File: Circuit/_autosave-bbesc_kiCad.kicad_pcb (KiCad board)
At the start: 2 copper layers, 81.4 x 63.5 mm, 82 parts, among them J1 CONN_01X06, J3 CONN_01X02, M3 -> 81.28mm MountingHole_3.2mm_M3_DIN965_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, M3 56.515mm Square MountingHole_3.2mm_M3_DIN965_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, M3 MountingHole_3.2mm_M3_DIN965_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, M3 offset inside by 3.429mm MountingHole_3.2mm_M3_DIN965_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, P2 CONN_01X03, P5 CONN_01X01, P6 CONN_01X01, P7 CONN_01X01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

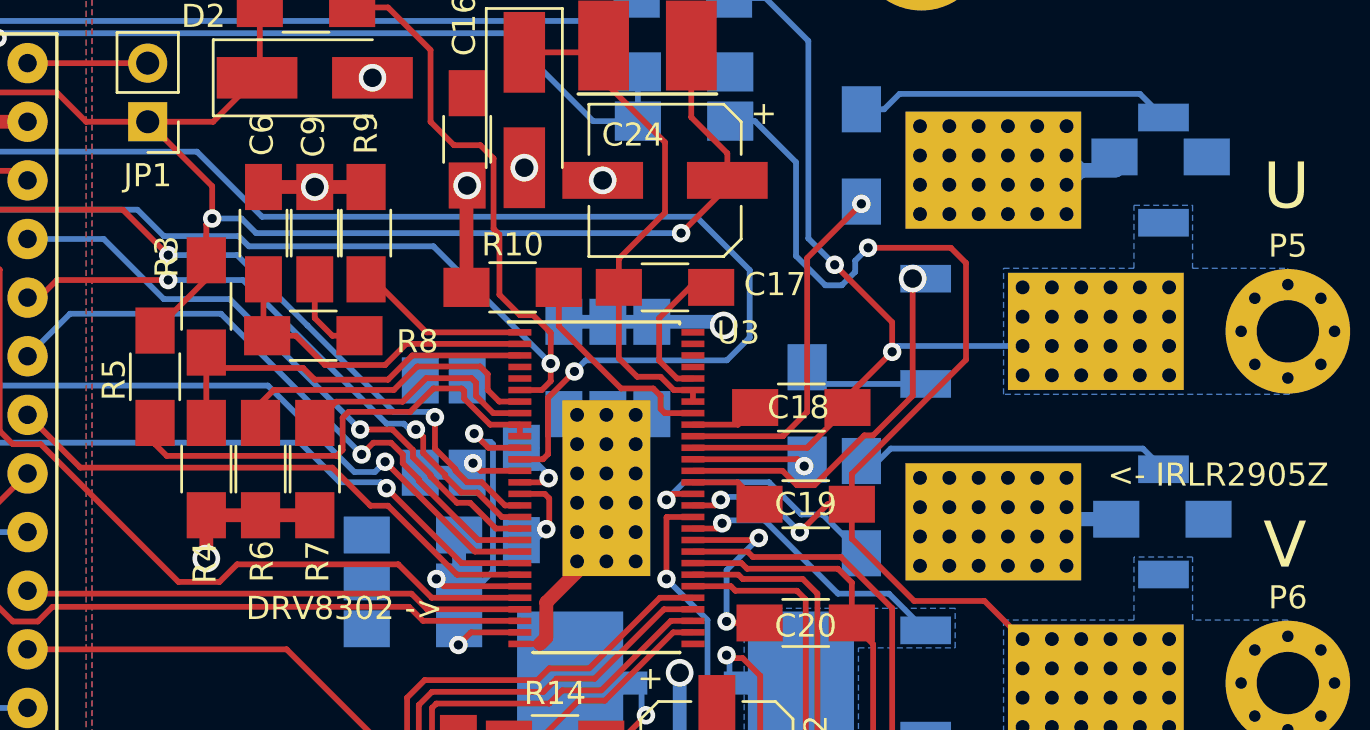
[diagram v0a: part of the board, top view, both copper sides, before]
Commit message: closed (encoder) loop 'voltage foc' with sinusoid pwm (discovered svpwm errors)
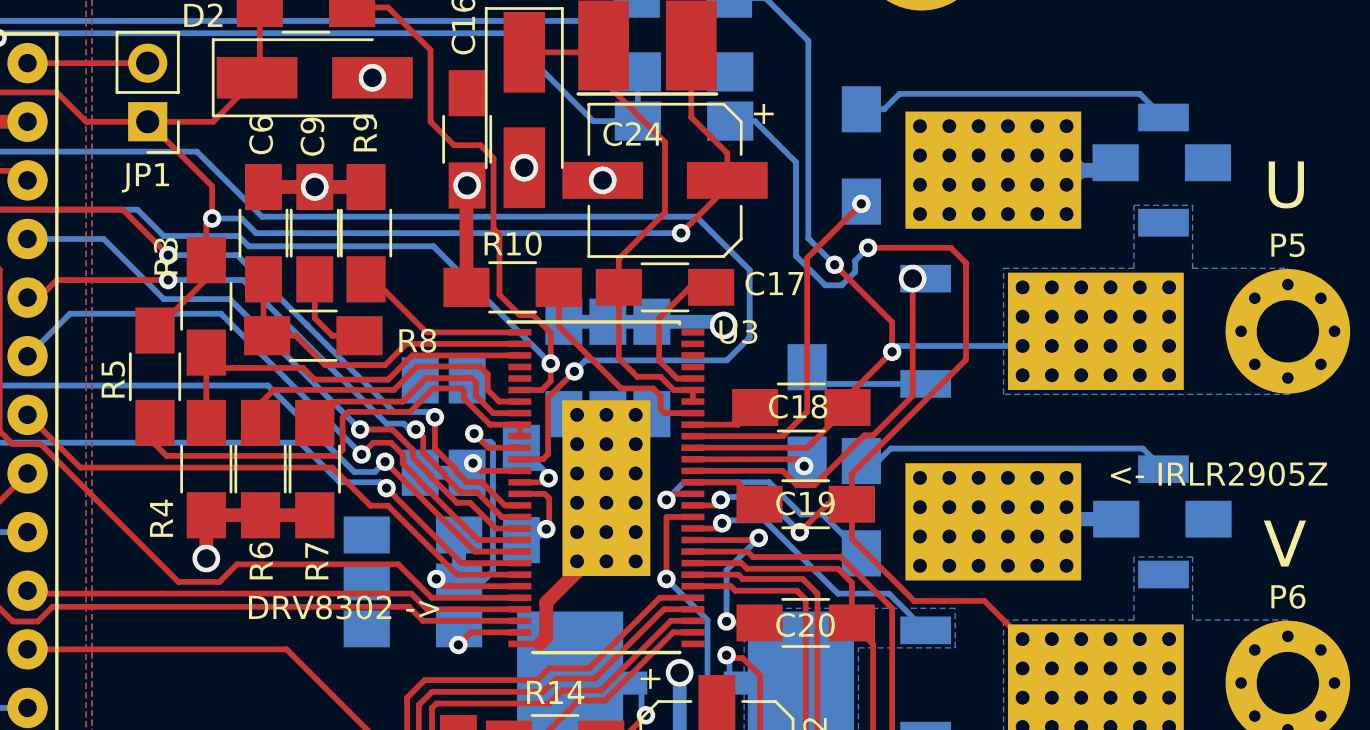
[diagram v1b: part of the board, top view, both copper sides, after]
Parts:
- moved C26 0.26 mm to (167.3, 79.9)
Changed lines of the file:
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@@
     (links 327)
     (no_connects 4)
-    (area 80.240287 47.592 192.762 143.67)
+    (area 96.825999 66.980999 178.383001 130.631001)
     (thickness 1.6)
     (drawings 26)
@@
     (visible_elements 7FFEFF7F)
     (pcbplotparams
-      (layerselection 0x011f0_80000001)
+      (layerselection 0x010f0_80000001)
       (usegerberextensions false)
       (excludeedgelayer true)
@@
       (viasonmask false)
       (mode 1)
-      (useauxorigin false)
+      (useauxorigin true)
       (hpglpennumber 1)
       (hpglpenspeed 20)
@@
       (padsonsilk false)
       (subtractmaskfromsilk false)
-      (outputformat 4)
+      (outputformat 1)
       (mirror false)
       (drillshape 0)
       (scaleselection 1)
-      (outputdirectory ../Documentation/))
+      (outputdirectory bbesc_Gerber/4fab/))
   )
   (net 0 "")
@@
   )
   (module Capacitors_SMD:C_1206_HandSoldering (layer B.Cu)
-    (at 167.2082 79.629)
+    (at 167.259 79.883)
     (descr "Capacitor SMD 1206, hand soldering")
     (tags "capacitor 1206")
@@
     (tags "resistor 1206")
     (attr smd)
-    (fp_text reference R4 (at -4.064 -0.0635 90) (layer F.SilkS)
-      (effects (font (size 1 1) (thickness 0.15)))
-    )
+    (fp_text reference R4 (at -2.159 -1.905 90) (layer F.SilkS)
+      (effects (font (size 1 1) (thickness 0.15)))
+    )
